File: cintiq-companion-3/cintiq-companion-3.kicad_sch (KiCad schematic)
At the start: 0 parts

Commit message: Schematic in an ok state
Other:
- sheet Mu ports: added none; removed DDI_B_AUX+, DDI_B_AUX-, DDI_B_DDC_SCL, DDI_B_DDC_SDA, DDI_B_HPD, DDI_B_TX0+, DDI_B_TX0-, DDI_B_TX1+, DDI_B_TX1-, DDI_B_TX2+, DDI_B_TX2-, DDI_B_TX3+, DDI_B_TX3-, FAN_1_PWM, FAN_1_TAC, HSIO_0_RX+, HSIO_0_RX-, HSIO_0_TX+, HSIO_0_TX-, HSIO_10_RX+, HSIO_10_RX-, HSIO_10_TX+, HSIO_10_TX-, HSIO_11_RX+, HSIO_11_RX-, HSIO_11_TX+, HSIO_11_TX-, HSIO_1_RX+, HSIO_1_RX-, HSIO_1_TX+, HSIO_1_TX-, HSIO_2_RX+, HSIO_2_RX-, HSIO_2_TX+, HSIO_2_TX-, HSIO_3_RX+, HSIO_3_RX-, HSIO_3_TX+, HSIO_3_TX-, HSIO_6_RX+, HSIO_6_RX-, HSIO_6_TX+, HSIO_6_TX-, HSIO_8_RX+, HSIO_8_RX-, HSIO_8_TX+, HSIO_8_TX-, HSIO_9_RX+, HSIO_9_RX-, HSIO_9_TX+, HSIO_9_TX-, I2C2_SCL, I2C2_SDA, I2C3_SCL, I2C3_SDA, I2C4_SCL, I2C4_SDA, I2C5_SCL, I2C5_SDA, REFCLK0+, REFCLK0-, REFCLK1+, REFCLK1-, REFCLK2+, REFCLK2-, REFCLK3+, REFCLK3-, REFCLK4+, REFCLK4-, SLS_S3, SOC_UART0_RX, SOC_UART0_TX, SOC_UART1_RX, SOC_UART1_TX, SOC_UART2_RX, SOC_UART2_TX, SUSCLK_WIFI, TCP0_AUX+, TCP0_AUX-, TCP0_DDC_SCL, TCP0_DDC_SDA, TCP0_HPD, TCP0_TX0+, TCP0_TX0-, TCP0_TX1+, TCP0_TX1-, TCP0_TXRX0+, TCP0_TXRX0-, TCP0_TXRX1+, TCP0_TXRX1-, TCP1_AUX+, TCP1_AUX-, TCP1_DDC_SCL, TCP1_DDC_SDA, TCP1_HPD, TCP1_TX0+, TCP1_TX0-, TCP1_TX1+, TCP1_TX1-, TCP1_TXRX0+, TCP1_TXRX0-, TCP1_TXRX1+, TCP1_TXRX1-, USB_2_P1+, USB_2_P1-, USB_2_P2+, USB_2_P2-, USB_2_P3+, USB_2_P3-, USB_2_P4+, USB_2_P4-, USB_2_P5+, USB_2_P5-, USB_2_P7+, USB_2_P7-, USB_2_P8+, USB_2_P8-, ~{PEWAKE}, ~{PLT_RST}, ~{PWR_LED}/~{PSON}, ~{PWR_SW}, ~{RST_SW}
- note added: "is this supposed to be a block diagram?"

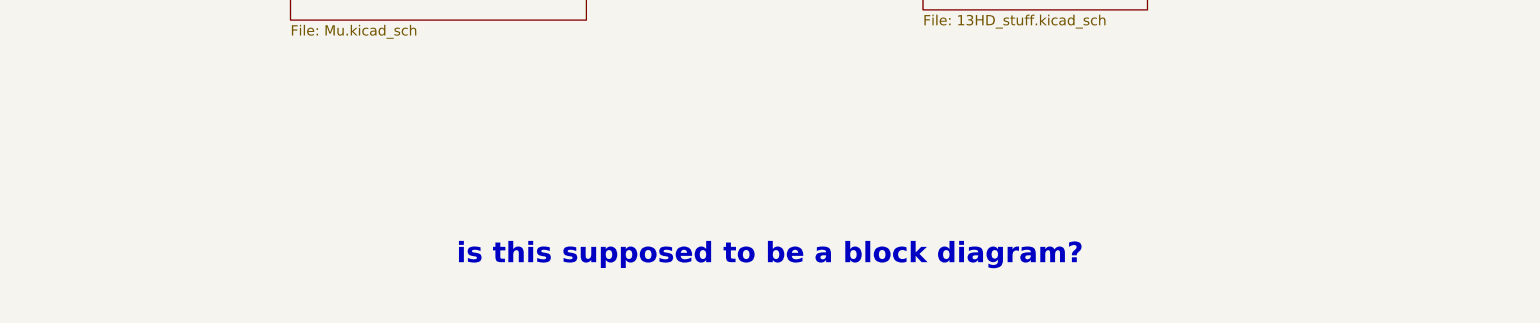
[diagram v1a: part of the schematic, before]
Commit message: Did some footprint assignments and added reference image to pcb editor
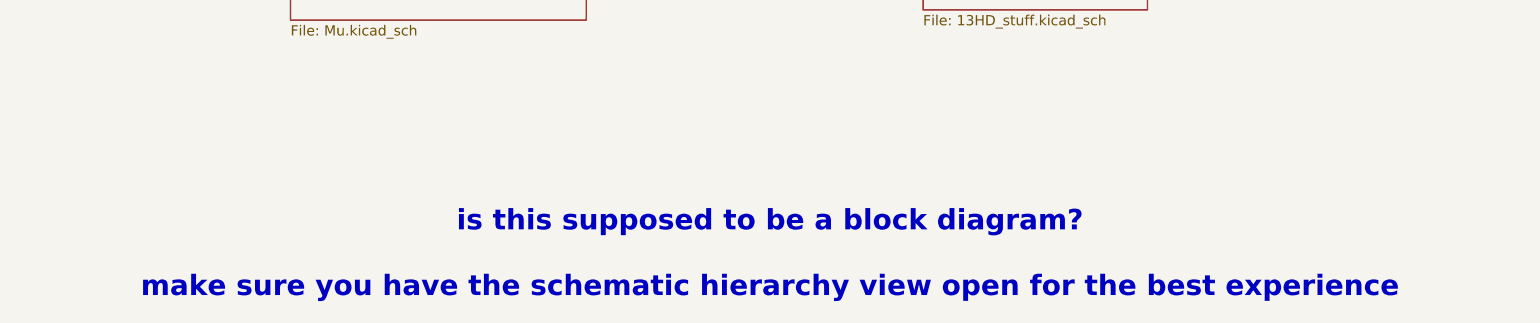
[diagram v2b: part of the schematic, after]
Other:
- note added: "is this supposed to be a block diagram? make sure you have the schematic hierarchy view open for the best experience"
- note removed: "is this supposed to be a block diagram?"
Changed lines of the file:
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@@
 		(company "WifiCable")
 	)
-	(text "is this supposed to be a block diagram?"
+	(text "is this supposed to be a block diagram?\n\nmake sure you have the schematic hierarchy view open for the best experience"
 		(exclude_from_sim no)
 		(at 149.86 133.35 0)

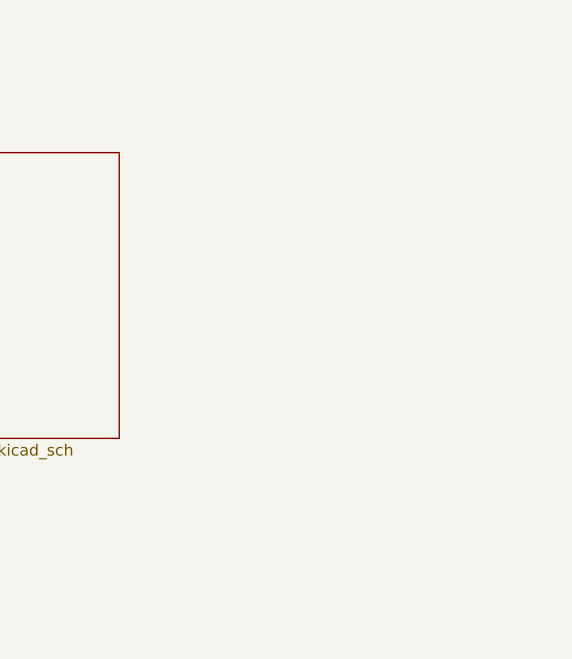
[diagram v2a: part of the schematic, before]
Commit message: Added m.2 ssd slot, did some test routing
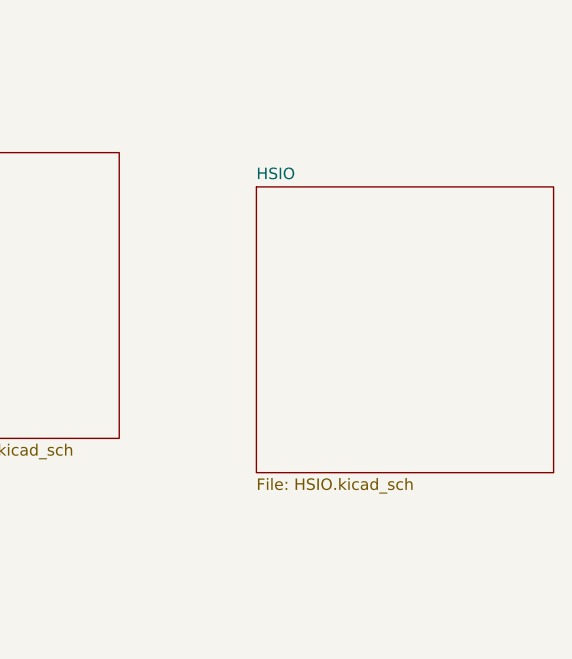
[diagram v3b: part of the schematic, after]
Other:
- added sheet HSIO (HSIO.kicad_sch)
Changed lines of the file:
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@@
+	)
+	(sheet
+		(at 212.09 74.93)
+		(size 33.02 31.75)
+		(fields_autoplaced yes)
+		(stroke
+			(width 0.1524)
+			(type solid)
+		)
+		(fill
+			(color 0 0 0 0.0000)
+		)
+		(property "Sheetname" "HSIO"
+			(at 212.09 74.2184 0)
+			(effects
+				(font
+					(size 1.27 1.27)
+				)
+				(justify left bottom)
+			)
+		)
+		(property "Sheetfile" "HSIO.kicad_sch"
+			(at 212.09 107.2646 0)
+			(effects
+				(font
+					(size 1.27 1.27)
+				)
+				(justify left top)
+			)
+		)
+		(instances
+			(project "cintiq-companion-3"
+				(path "/ef92970f-f7a1-4011-9c13-6d46a45b923d"
+					(page "4")
+				)
+			)
+		)
 	)
 	(sheet

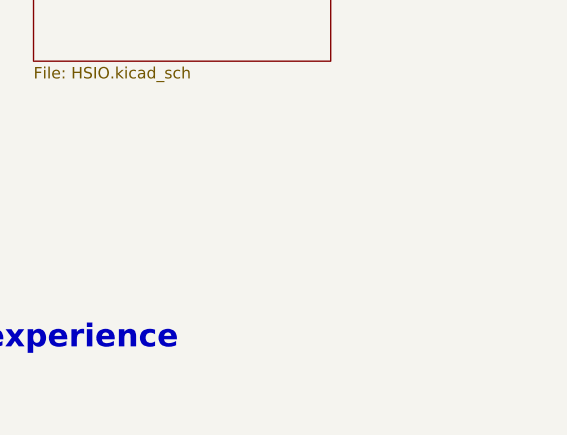
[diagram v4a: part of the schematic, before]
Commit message: Added B-key slot and dual bios chips
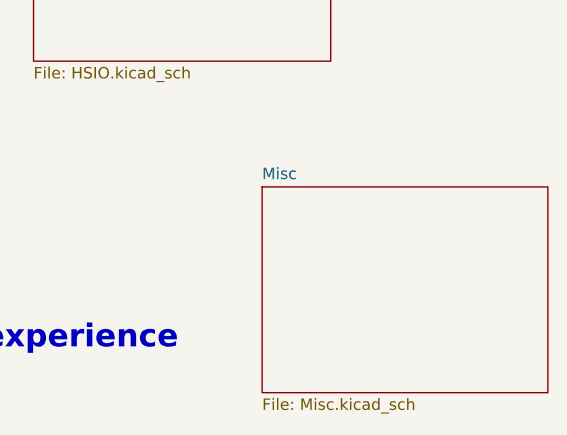
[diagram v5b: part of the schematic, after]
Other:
- added sheet Misc (Misc.kicad_sch)
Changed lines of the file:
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@@
+		)
+	)
+	(sheet
+		(at 237.49 120.65)
+		(size 31.75 22.86)
+		(fields_autoplaced yes)
+		(stroke
+			(width 0.1524)
+			(type solid)
+		)
+		(fill
+			(color 0 0 0 0.0000)
+		)
+		(property "Sheetname" "Misc"
+			(at 237.49 119.9384 0)
+			(effects
+				(font
+					(size 1.27 1.27)
+				)
+				(justify left bottom)
+			)
+		)
+		(property "Sheetfile" "Misc.kicad_sch"
+			(at 237.49 144.0946 0)
+			(effects
+				(font
+					(size 1.27 1.27)
+				)
+				(justify left top)
+			)
+		)
+		(instances
+			(project "cintiq-companion-3"
+				(path "/ef92970f-f7a1-4011-9c13-6d46a45b923d"
+					(page "5")
+				)
+			)
 		)
 	)

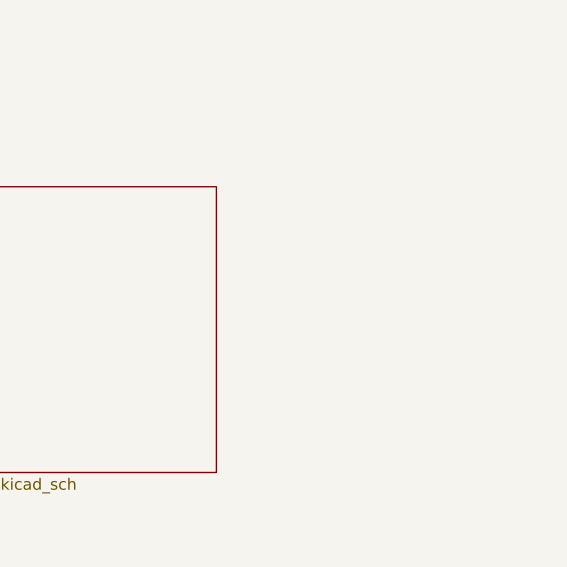
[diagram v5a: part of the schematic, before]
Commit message: Started adding type-c
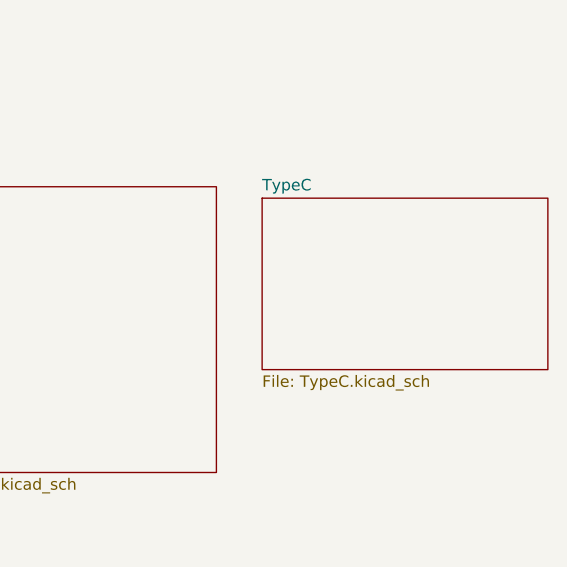
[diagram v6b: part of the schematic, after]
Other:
- added sheet TypeC (TypeC.kicad_sch)
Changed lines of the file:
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@@
+	)
+	(sheet
+		(at 250.19 76.2)
+		(size 31.75 19.05)
+		(fields_autoplaced yes)
+		(stroke
+			(width 0.1524)
+			(type solid)
+		)
+		(fill
+			(color 0 0 0 0.0000)
+		)
+		(property "Sheetname" "TypeC"
+			(at 250.19 75.4884 0)
+			(effects
+				(font
+					(size 1.27 1.27)
+				)
+				(justify left bottom)
+			)
+		)
+		(property "Sheetfile" "TypeC.kicad_sch"
+			(at 250.19 95.8346 0)
+			(effects
+				(font
+					(size 1.27 1.27)
+				)
+				(justify left top)
+			)
+		)
+		(instances
+			(project "cintiq-companion-3"
+				(path "/ef92970f-f7a1-4011-9c13-6d46a45b923d"
+					(page "5")
+				)
+			)
+		)
 	)
 	(sheet
@@
 			(project "cintiq-companion-3"
 				(path "/ef92970f-f7a1-4011-9c13-6d46a45b923d"
-					(page "5")
+					(page "6")
 				)
 			)
